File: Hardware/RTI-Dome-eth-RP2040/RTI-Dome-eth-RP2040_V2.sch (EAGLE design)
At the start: 106 parts, among them IC1 REG1117FA-5.0_500, IC2 24LC64T-I/SN, IC3 FT232RL, IC4 RASPBERRY_PI_PICO, IC8 REG1117-3.3V, J2 XT60PW-M, T1 MMBT3904LT1, T2 MMBT3904LT1, T3 MMBT3904LT1, U1 W5500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

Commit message: Added a few things to the V2 board
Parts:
- added Q1: DMG2305UX-7, samacsys:DMG2305UX-7
- added S1: EVQ-P2H02B, samacsys:EVQ-P2H02B
- IC4: value RASPBERRY_PI_PICO -> RASPBERRY_PI_PICOW; device samacsys:RASPBERRY_PI_PICO -> samacsys:RASPBERRY_PI_PICOW; DESCRIPTION RASPBERRY-PI - RASPBERRY PI PICO - Raspberry Pi Board, Rasp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 -> (none); MANUFACTURER_NAME RASPBERRY-PI PICO -> (none); MANUFACTURER_PART_NUMBER SC0916 -> (none); MOUSER_PART_NUMBER SC0915 -> (none); MPN SC0916 -> (none)
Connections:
- new net VSYS: IC4.VSYS, Q1.S
- net GND: now also S1.COM_1, S1.COM_2
- net RESET: now also S1.NO_2
- net VBUS: now also Q1.G
- net VCC: now also Q1.D; no longer IC4.VSYS
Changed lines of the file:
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@@
 <part name="FRAME2" library="frames" library_urn="urn:adsk.eagle:library:229" deviceset="DINA3_L" device=""/>
 <part name="GND16" library="supply1" library_urn="urn:adsk.eagle:library:371" deviceset="GND" device=""/>
-<part name="J2" library="samacsys" library_urn="urn:adsk.eagle:library:37256869" deviceset="XT60PW-M" device="" package3d_urn="urn:adsk.eagle:package:37256940/5"/>
+<part name="J2" library="samacsys" library_urn="urn:adsk.eagle:library:37256869" deviceset="XT60PW-M" device="" package3d_urn="urn:adsk.eagle:package:37256940/7"/>
 <part name="X2" library="rti" library_urn="urn:adsk.eagle:library:37256580" deviceset="AK500/3" device="" package3d_urn="urn:adsk.eagle:package:37500967/6"/>
 <part name="X10" library="rti" library_urn="urn:adsk.eagle:library:37256580" deviceset="AK500/3" device="" package3d_urn="urn:adsk.eagle:package:37500967/6"/>
@@
 </part>
 <part name="GND38" library="supply1" library_urn="urn:adsk.eagle:library:371" deviceset="GND" device=""/>
-<part name="IC4" library="samacsys" library_urn="urn:adsk.eagle:library:37256869" deviceset="RASPBERRY_PI_PICO" device="" package3d_urn="urn:adsk.eagle:package:40546189/7" value="RASPBERRY_PI_PICO">
-<attribute name="DESCRIPTION" value="RASPBERRY-PI - RASPBERRY PI PICO - Raspberry Pi Board, Raspberry Pi Pic, RP2040, 32bit, ARM Cortex-M0+"/>
+<part name="IC4" library="samacsys" library_urn="urn:adsk.eagle:library:37256869" deviceset="RASPBERRY_PI_PICO" device="W" package3d_urn="urn:adsk.eagle:package:44159720/2" value="RASPBERRY_PI_PICOW">
 <attribute name="JLCPCBPN" value="C7203003"/>
-<attribute name="MANUFACTURER_NAME" value="RASPBERRY-PI PICO"/>
-<attribute name="MANUFACTURER_PART_NUMBER" value="SC0916"/>
-<attribute name="MOUSER_PART_NUMBER" value="SC0915"/>
-<attribute name="MPN" value="SC0916"/>
 </part>
 <part name="X13" library="rti" library_urn="urn:adsk.eagle:library:37256580" deviceset="PN61729-S" device="" package3d_urn="urn:adsk.eagle:package:37504981/2">
@@
 <part name="IC1" library="REG1117FA-5.0_500" library_urn="urn:adsk.eagle:library:43937876" deviceset="REG1117FA-5.0_500" device="" package3d_urn="urn:adsk.eagle:package:43937879/3"/>
 <part name="GND3" library="supply1" library_urn="urn:adsk.eagle:library:371" deviceset="GND" device=""/>
+<part name="S1" library="samacsys" library_urn="urn:adsk.eagle:library:37256869" deviceset="EVQ-P2H02B" device="" package3d_urn="urn:adsk.eagle:package:44159643/2"/>
+<part name="GND8" library="supply1" library_urn="urn:adsk.eagle:library:371" deviceset="GND" device=""/>
+<part name="Q1" library="samacsys" library_urn="urn:adsk.eagle:library:37256869" deviceset="DMG2305UX-7" device="" package3d_urn="urn:adsk.eagle:package:44159710/2"/>
 </parts>
 <sheets>
@@
 <attribute name="VALUE" x="250.444" y="100.711" size="1.778" layer="96"/>
 </instance>
-<instance part="GND2" gate="1" x="248.92" y="97.79" smashed="yes">
-<attribute name="VALUE" x="246.38" y="95.25" size="1.778" layer="96"/>
+<instance part="GND2" gate="1" x="248.92" y="95.25" smashed="yes">
+<attribute name="VALUE" x="246.38" y="92.71" size="1.778" layer="96"/>
 </instance>
 <instance part="R5" gate="G$1" x="241.3" y="110.49" smashed="yes" rot="R180">
@@
 <attribute name="VALUE" x="252.984" y="67.691" size="1.778" layer="96"/>
 </instance>
-<instance part="GND34" gate="1" x="251.46" y="64.77" smashed="yes">
-<attribute name="VALUE" x="248.92" y="62.23" size="1.778" layer="96"/>
+<instance part="GND34" gate="1" x="251.46" y="62.23" smashed="yes">
+<attribute name="VALUE" x="248.92" y="59.69" size="1.778" layer="96"/>
 </instance>
 <instance part="R47" gate="G$1" x="241.3" y="166.37" smashed="yes" rot="R180">
@@
 <attribute name="NAME" x="83.82" y="68.58" size="1.778" layer="95" align="center-left"/>
 <attribute name="VALUE" x="83.82" y="66.04" size="1.778" layer="96" align="center-left"/>
-<attribute name="MPN" x="109.22" y="40.64" size="1.778" layer="96" display="off"/>
 <attribute name="JLCPCBPN" x="109.22" y="40.64" size="1.778" layer="96" display="off"/>
 </instance>
@@
 <instance part="GND3" gate="1" x="31.75" y="128.27" smashed="yes">
 <attribute name="VALUE" x="29.21" y="125.73" size="1.778" layer="96"/>
+</instance>
+<instance part="S1" gate="G$1" x="203.2" y="36.83" smashed="yes">
+<attribute name="NAME" x="201.93" y="43.18" size="1.778" layer="95" align="center-left"/>
+<attribute name="VALUE" x="198.12" y="31.75" size="1.778" layer="96" align="center-left"/>
+</instance>
+<instance part="GND8" gate="1" x="222.25" y="30.48" smashed="yes">
+<attribute name="VALUE" x="219.71" y="27.94" size="1.778" layer="96"/>
+</instance>
+<instance part="Q1" gate="G$1" x="171.45" y="69.85" smashed="yes" rot="R90">
+<attribute name="NAME" x="170.18" y="74.93" size="1.778" layer="95" rot="R90" align="center-left"/>
+<attribute name="VALUE" x="172.72" y="74.93" size="1.778" layer="96" rot="R90" align="center-left"/>
 </instance>
 </instances>
@@
 <pinref part="C1" gate="G$1" pin="2"/>
 <pinref part="GND2" gate="1" pin="GND"/>
+<wire x1="248.92" y1="97.79" x2="248.92" y2="100.33" width="0.1524" layer="91"/>
 </segment>
 <segment>
@@
 <pinref part="GND34" gate="1" pin="GND"/>
 <pinref part="C42" gate="G$1" pin="2"/>
+<wire x1="251.46" y1="64.77" x2="251.46" y2="67.31" width="0.1524" layer="91"/>
 </segment>
 <segment>
@@
 <wire x1="31.75" y1="132.08" x2="53.34" y2="132.08" width="0.1524" layer="91"/>
 <wire x1="53.34" y1="132.08" x2="53.34" y2="133.35" width="0.1524" layer="91"/>
+</segment>
+<segment>
+<pinref part="S1" gate="G$1" pin="COM_1"/>
+<wire x1="219.71" y1="38.1" x2="222.25" y2="38.1" width="0.1524" layer="91"/>
+<wire x1="222.25" y1="38.1" x2="222.25" y2="35.56" width="0.1524" layer="91"/>
+<pinref part="S1" gate="G$1" pin="COM_2"/>
+<wire x1="222.25" y1="35.56" x2="222.25" y2="33.02" width="0.1524" layer="91"/>
+<wire x1="219.71" y1="35.56" x2="222.25" y2="35.56" width="0.1524" layer="91"/>
+<junction x="222.25" y="35.56"/>
+<pinref part="GND8" gate="1" pin="GND"/>
 </segment>
 </net>
@@
 </segment>
 <segment>
-<pinref part="IC4" gate="G$1" pin="VSYS"/>
-<wire x1="161.29" y1="58.42" x2="158.75" y2="58.42" width="0.1524" layer="91"/>
-<label x="161.29" y="58.42" size="1.016" layer="95" xref="yes"/>
-</segment>
-<segment>
 <pinref part="X6" gate="-3" pin="KL"/>
 <wire x1="295.91" y1="186.69" x2="298.45" y2="186.69" width="0.1524" layer="91"/>
@@
 <pinref part="C28" gate="G$1" pin="1"/>
 </segment>
+<segment>
+<pinref part="Q1" gate="G$1" pin="D"/>
+<wire x1="160.02" y1="71.12" x2="163.83" y2="71.12" width="0.1524" layer="91"/>
+<label x="160.02" y="71.12" size="1.016" layer="95" rot="R180" xref="yes"/>
+</segment>
 </net>
 <net name="N$2" class="0">
@@
 <label x="161.29" y="35.56" size="1.016" layer="95" xref="yes"/>
 </segment>
+<segment>
+<pinref part="S1" gate="G$1" pin="NO_2"/>
+<wire x1="189.23" y1="35.56" x2="186.69" y2="35.56" width="0.1524" layer="91"/>
+<label x="186.69" y="35.56" size="1.016" layer="95" rot="R180" xref="yes"/>
+</segment>
 </net>
 <net name="FTDI_RESET" class="0">
@@
 </segment>
 </net>
-<net name="VBUS" class="0">
-<segment>
-<pinref part="IC4" gate="G$1" pin="VBUS"/>
-<wire x1="161.29" y1="60.96" x2="158.75" y2="60.96" width="0.1524" layer="91"/>
-<label x="161.29" y="60.96" size="1.016" layer="95" xref="yes"/>
-</segment>
-</net>
 <net name="USB_VCC" class="0">
 <segment>
@@
 </segment>
 </net>
+<net name="VBUS" class="0">
+<segment>
+<pinref part="IC4" gate="G$1" pin="VBUS"/>
+<pinref part="Q1" gate="G$1" pin="G"/>
+<wire x1="158.75" y1="60.96" x2="173.99" y2="60.96" width="0.1524" layer="91"/>
+<wire x1="173.99" y1="60.96" x2="173.99" y2="63.5" width="0.1524" layer="91"/>
+</segment>
+</net>
+<net name="VSYS" class="0">
+<segment>
+<pinref part="Q1" gate="G$1" pin="S"/>
+<wire x1="179.07" y1="71.12" x2="182.88" y2="71.12" width="0.1524" layer="91"/>
+<wire x1="182.88" y1="71.12" x2="182.88" y2="58.42" width="0.1524" layer="91"/>
+<pinref part="IC4" gate="G$1" pin="VSYS"/>
+<wire x1="182.88" y1="58.42" x2="158.75" y2="58.42" width="0.1524" layer="91"/>
+</segment>
+</net>

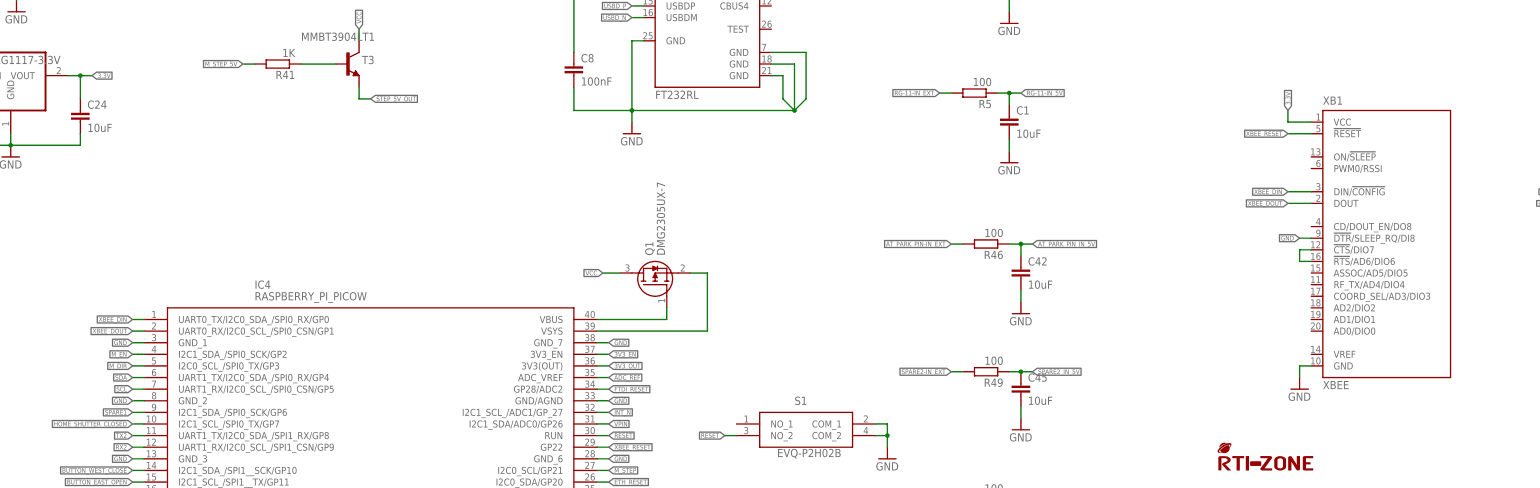
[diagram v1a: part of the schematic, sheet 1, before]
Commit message: Removed XBee from RP2040 boards as they'll use WiFi
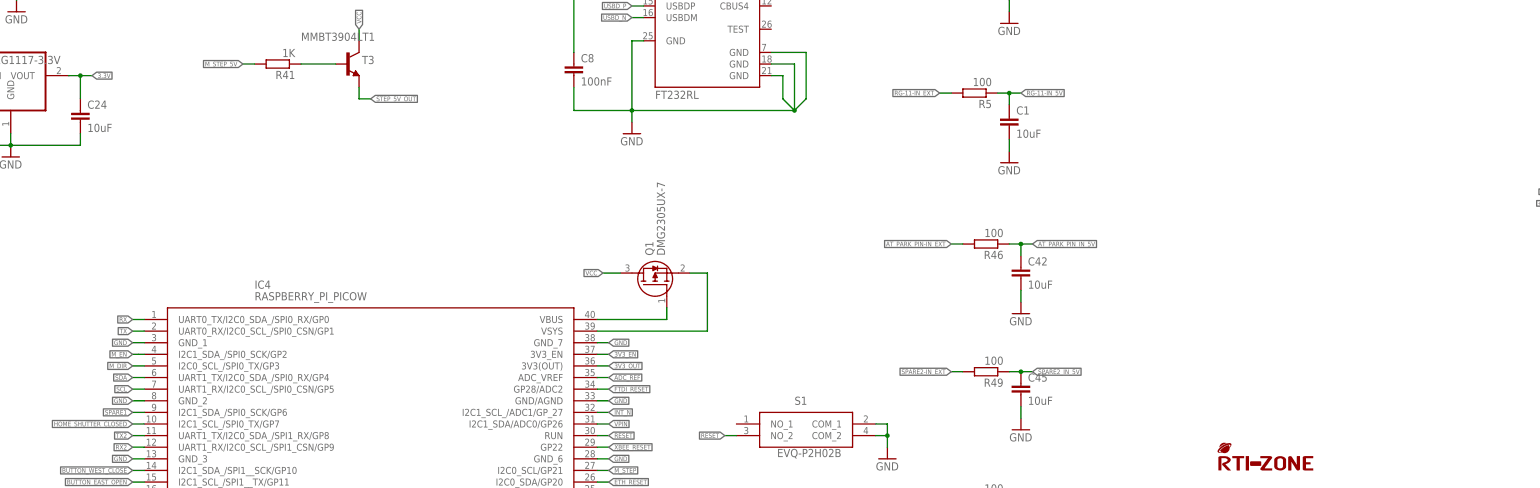
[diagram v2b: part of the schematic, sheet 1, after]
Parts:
- removed XB1: XBEE, rti:XBEE
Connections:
- removed net N$9: XB1.!CTS!/DIO7, XB1.!RTS!/AD6/DIO6
- removed net XBEE_DIN: IC4.UART0_TX/I2C0_SDA_/SPI0_RX/GP0, XB1.DIN/!CONFIG
- removed net XBEE_DOUT: IC4.UART0_RX/I2C0_SCL_/SPI0_CSN/GP1, XB1.DOUT
- new net RX: IC4.UART0_TX/I2C0_SDA_/SPI0_RX/GP0
- new net TX: IC4.UART0_RX/I2C0_SCL_/SPI0_CSN/GP1
- net 3.3V: no longer XB1.VCC
- net GND: no longer XB1.!DTR!/SLEEP_RQ/DI8, XB1.GND
- net XBEE_RESET: no longer XB1.!RESET
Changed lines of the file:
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@@
 </part>
 <part name="GND1" library="supply1" library_urn="urn:adsk.eagle:library:371" deviceset="GND" device=""/>
-<part name="XB1" library="rti" library_urn="urn:adsk.eagle:library:37256580" deviceset="XBEE" device="" package3d_urn="urn:adsk.eagle:package:37505126/2"/>
-<part name="GND6" library="supply1" library_urn="urn:adsk.eagle:library:371" deviceset="GND" device=""/>
 <part name="R2" library="rcl" library_urn="urn:adsk.eagle:library:334" deviceset="R-EU_" device="R0603" package3d_urn="urn:adsk.eagle:package:23555/3" value="100K 0.1%">
 <spice>
@@
 <attribute name="VALUE" x="119.38" y="182.88" size="1.778" layer="96"/>
 </instance>
-<instance part="XB1" gate="G$1" x="330.2" y="78.74" smashed="yes">
-<attribute name="NAME" x="317.5" y="107.95" size="1.778" layer="95"/>
-<attribute name="VALUE" x="317.5" y="45.72" size="1.778" layer="96"/>
-</instance>
-<instance part="GND6" gate="1" x="312.42" y="45.72" smashed="yes">
-<attribute name="VALUE" x="309.88" y="43.18" size="1.778" layer="96"/>
-</instance>
 <instance part="R2" gate="G$1" x="7.62" y="213.36" smashed="yes" rot="R90">
 <attribute name="MPN" x="7.62" y="213.36" size="1.778" layer="96" rot="R90" display="off"/>
@@
 <junction x="116.84" y="190.5"/>
 <pinref part="U$3" gate="G$2" pin="GND"/>
-</segment>
-<segment>
-<pinref part="XB1" gate="G$1" pin="!DTR!/SLEEP_RQ/DI8"/>
-<wire x1="312.42" y1="78.74" x2="314.96" y2="78.74" width="0.1524" layer="91"/>
-<label x="312.42" y="78.74" size="1.016" layer="95" rot="R180" xref="yes"/>
-</segment>
-<segment>
-<pinref part="XB1" gate="G$1" pin="GND"/>
-<wire x1="314.96" y1="50.8" x2="312.42" y2="50.8" width="0.1524" layer="91"/>
-<wire x1="312.42" y1="50.8" x2="312.42" y2="48.26" width="0.1524" layer="91"/>
-<pinref part="GND6" gate="1" pin="GND"/>
 </segment>
 <segment>
@@
 <junction x="116.84" y="210.82"/>
 <pinref part="U$3" gate="G$2" pin="VCC"/>
-</segment>
-<segment>
-<wire x1="309.88" y1="106.68" x2="309.88" y2="104.14" width="0.1524" layer="91"/>
-<pinref part="XB1" gate="G$1" pin="VCC"/>
-<wire x1="309.88" y1="104.14" x2="314.96" y2="104.14" width="0.1524" layer="91"/>
-<label x="309.88" y="106.68" size="1.016" layer="95" rot="R90" xref="yes"/>
 </segment>
 <segment>
@@
 </segment>
 </net>
-<net name="XBEE_DIN" class="0">
-<segment>
-<pinref part="XB1" gate="G$1" pin="DIN/!CONFIG"/>
-<wire x1="309.88" y1="88.9" x2="314.96" y2="88.9" width="0.1524" layer="91"/>
-<label x="309.88" y="88.9" size="1.016" layer="95" ratio="4" rot="R180" xref="yes"/>
-</segment>
+<net name="RX" class="0">
 <segment>
 <pinref part="IC4" gate="G$1" pin="UART0_TX/I2C0_SDA_/SPI0_RX/GP0"/>
@@
 </segment>
 </net>
-<net name="XBEE_DOUT" class="0">
-<segment>
-<pinref part="XB1" gate="G$1" pin="DOUT"/>
-<wire x1="309.88" y1="86.36" x2="314.96" y2="86.36" width="0.1524" layer="91"/>
-<label x="309.88" y="86.36" size="1.016" layer="95" ratio="4" rot="R180" xref="yes"/>
-</segment>
+<net name="TX" class="0">
 <segment>
 <pinref part="IC4" gate="G$1" pin="UART0_RX/I2C0_SCL_/SPI0_CSN/GP1"/>
@@
 <net name="XBEE_RESET" class="0">
 <segment>
-<pinref part="XB1" gate="G$1" pin="!RESET"/>
-<wire x1="309.88" y1="101.6" x2="314.96" y2="101.6" width="0.1524" layer="91"/>
-<label x="309.88" y="101.6" size="1.016" layer="95" ratio="4" rot="R180" xref="yes"/>
-</segment>
-<segment>
 <pinref part="IC4" gate="G$1" pin="GP22"/>
 <wire x1="161.29" y1="33.02" x2="158.75" y2="33.02" width="0.1524" layer="91"/>
@@
 </segment>
 </net>
-<net name="N$9" class="0">
-<segment>
-<pinref part="XB1" gate="G$1" pin="!CTS!/DIO7"/>
-<wire x1="314.96" y1="76.2" x2="312.42" y2="76.2" width="0.1524" layer="91"/>
-<wire x1="312.42" y1="76.2" x2="312.42" y2="73.66" width="0.1524" layer="91"/>
-<pinref part="XB1" gate="G$1" pin="!RTS!/AD6/DIO6"/>
-<wire x1="312.42" y1="73.66" x2="314.96" y2="73.66" width="0.1524" layer="91"/>
-</segment>
-</net>
